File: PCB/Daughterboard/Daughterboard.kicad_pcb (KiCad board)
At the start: 2 copper layers, 40 x 35 mm, 8 parts, among them J1 Conn_01x03_Pin, J2 Conn_01x03_Pin, J3 Screw_Terminal_01x02, J4 Screw_Terminal_01x02, J5 Screw_Terminal_01x02

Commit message: pcb tweaks and new gerbers
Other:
- board text added: "DESIGNED BY SHAWN MALLUWA-WADU"

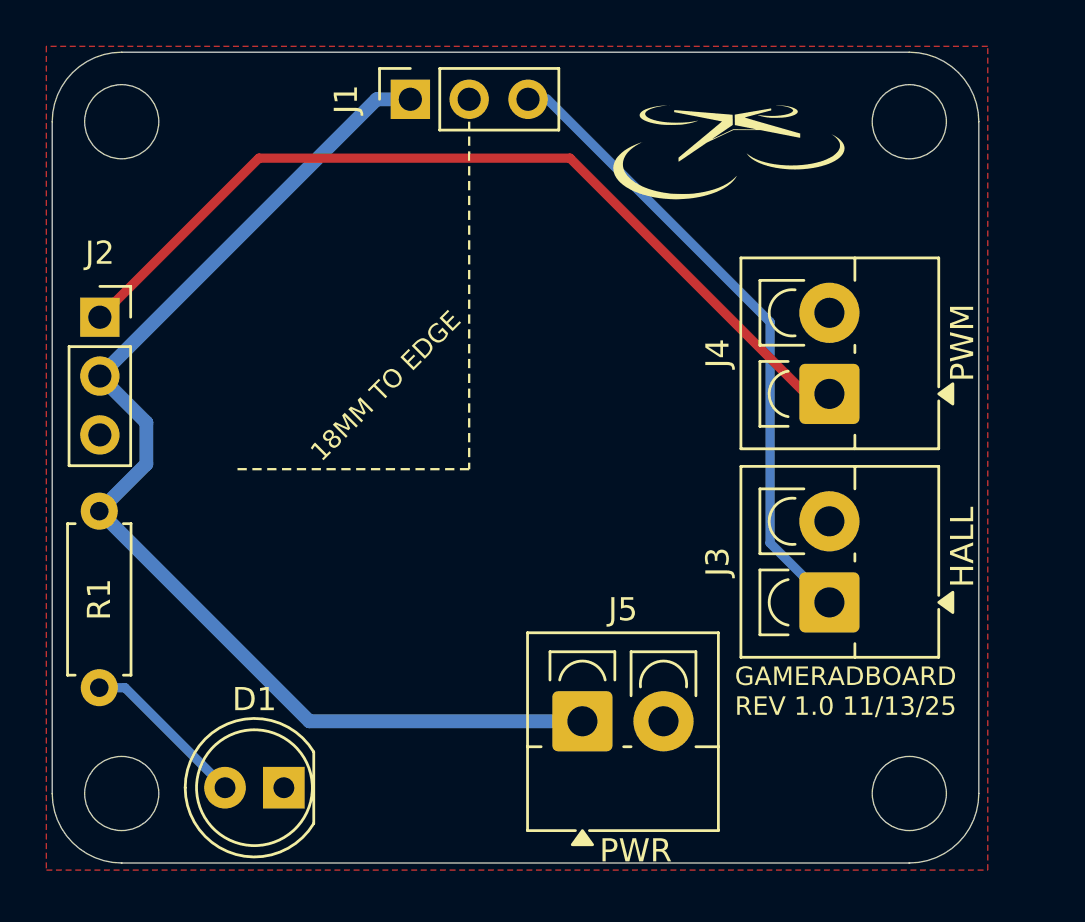
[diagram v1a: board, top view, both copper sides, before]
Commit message: refactored src for avionics with new things
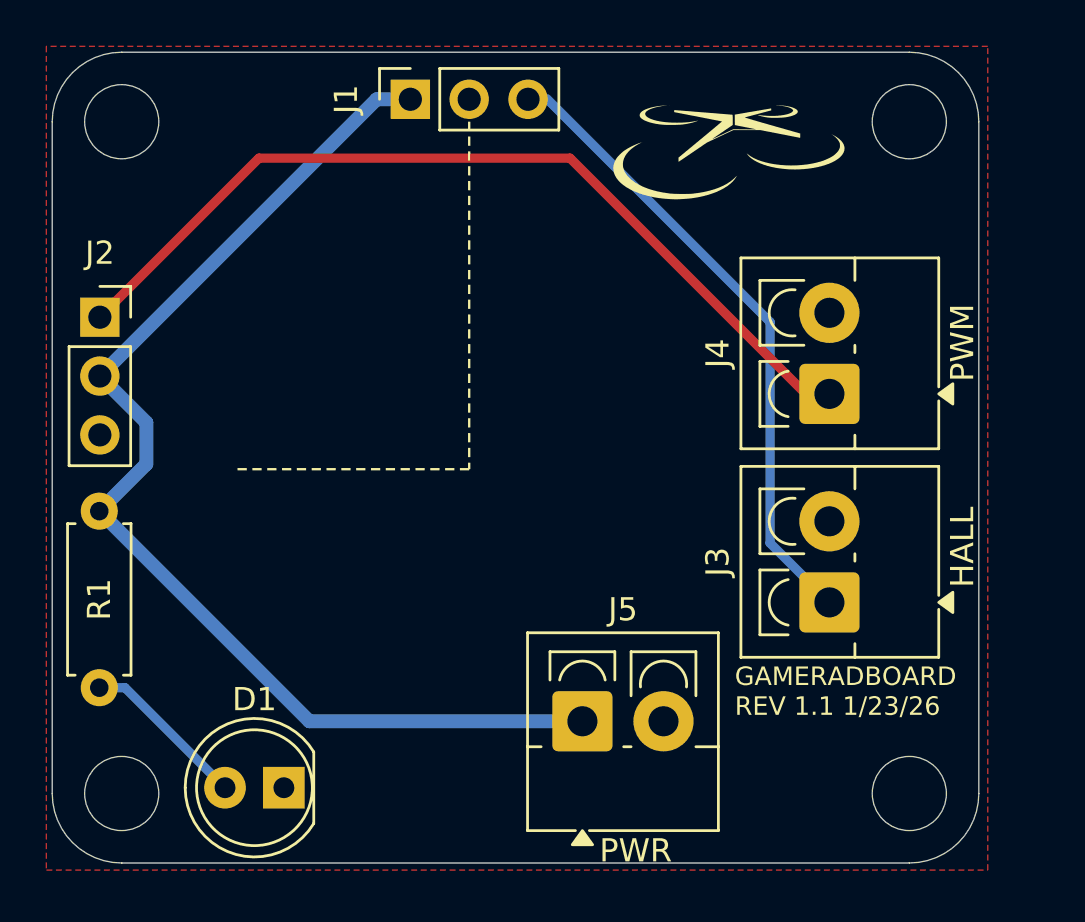
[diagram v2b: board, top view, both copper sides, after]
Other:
- board text added: "18mm to edge"
- board text added: "GAMERADBOARD REV 1.1 1/23/26"
- board text added: "SHAWNMALLUWAWADU@GMAIL.COM"
- board text removed: "18MM TO EDGE"
- board text removed: "GAMERADBOARD REV 1.0 11/13/25"
